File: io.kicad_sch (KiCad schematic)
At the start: 43 parts, among them J10 Conn_01x04_Socket, J11 CAN_TERMINATION, J2 Micro_SD_Card, J4 STM_USBC, J8 QT1, J9 QT2, U10 TCAN334G, U9 NUP4202

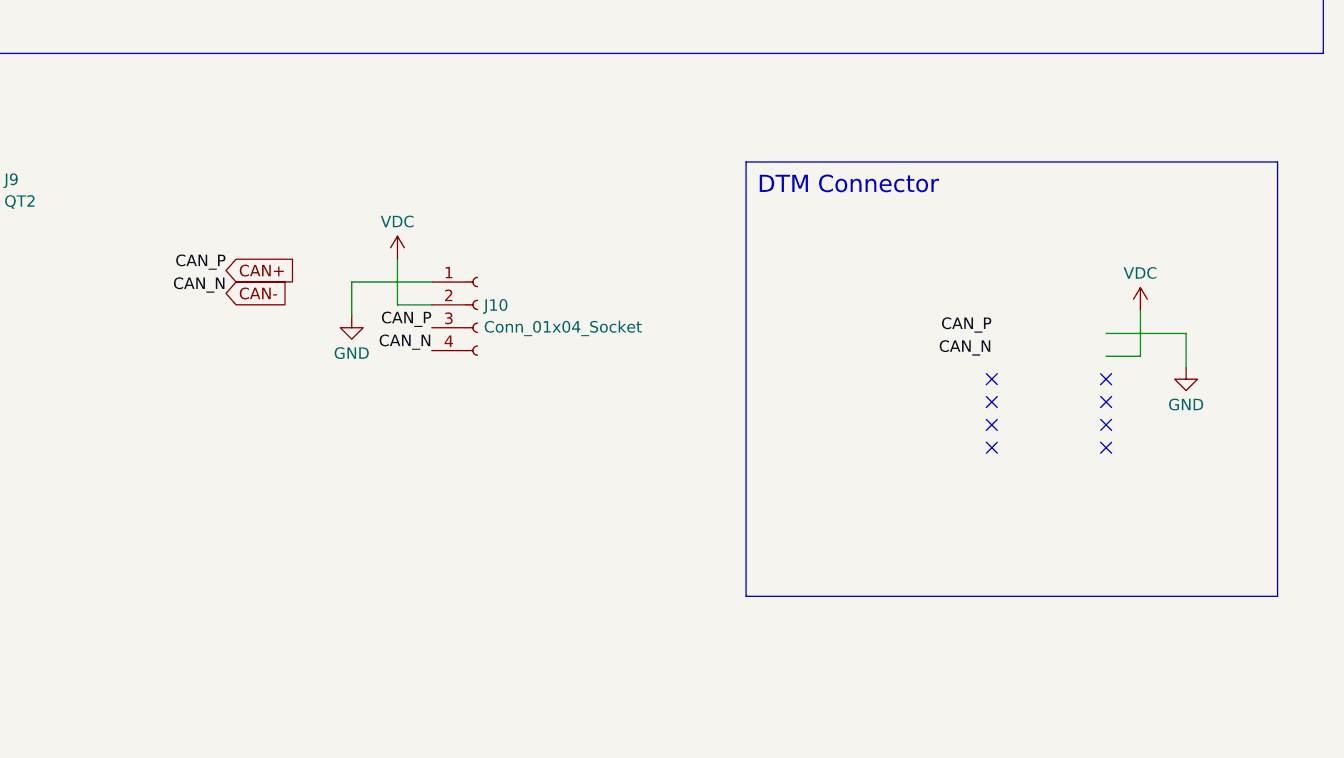
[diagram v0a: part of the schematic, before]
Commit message: minor schematic reorg
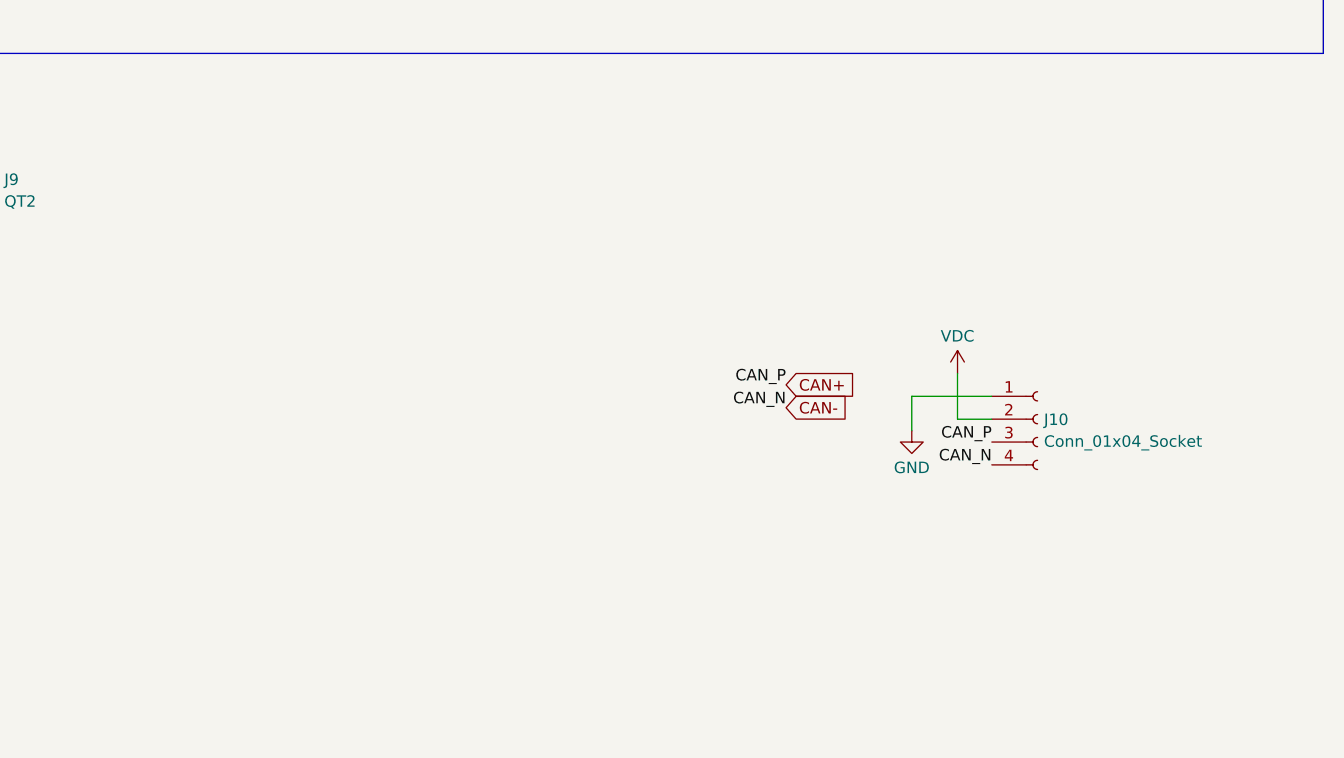
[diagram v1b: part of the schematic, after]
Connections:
- no-connect marks 10 -> 2
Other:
- note removed: "DTM Connector"
- moved on the sheet: J10
